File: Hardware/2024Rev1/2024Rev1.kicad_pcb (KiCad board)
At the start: 2 copper layers, 106.7 x 88.9 mm, 84 parts, among them J7 RJ45_LED_Shielded, Q2 BSS138, Q3 BSS138, Q5 BSS138, Q6 SPD30P06PGBTMA1, Q7 BSS138, U2 Opamp_Dual, U3 Teensy4.1_DEV-16771, U4 Opamp_Dual, U5 Opamp_Dual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

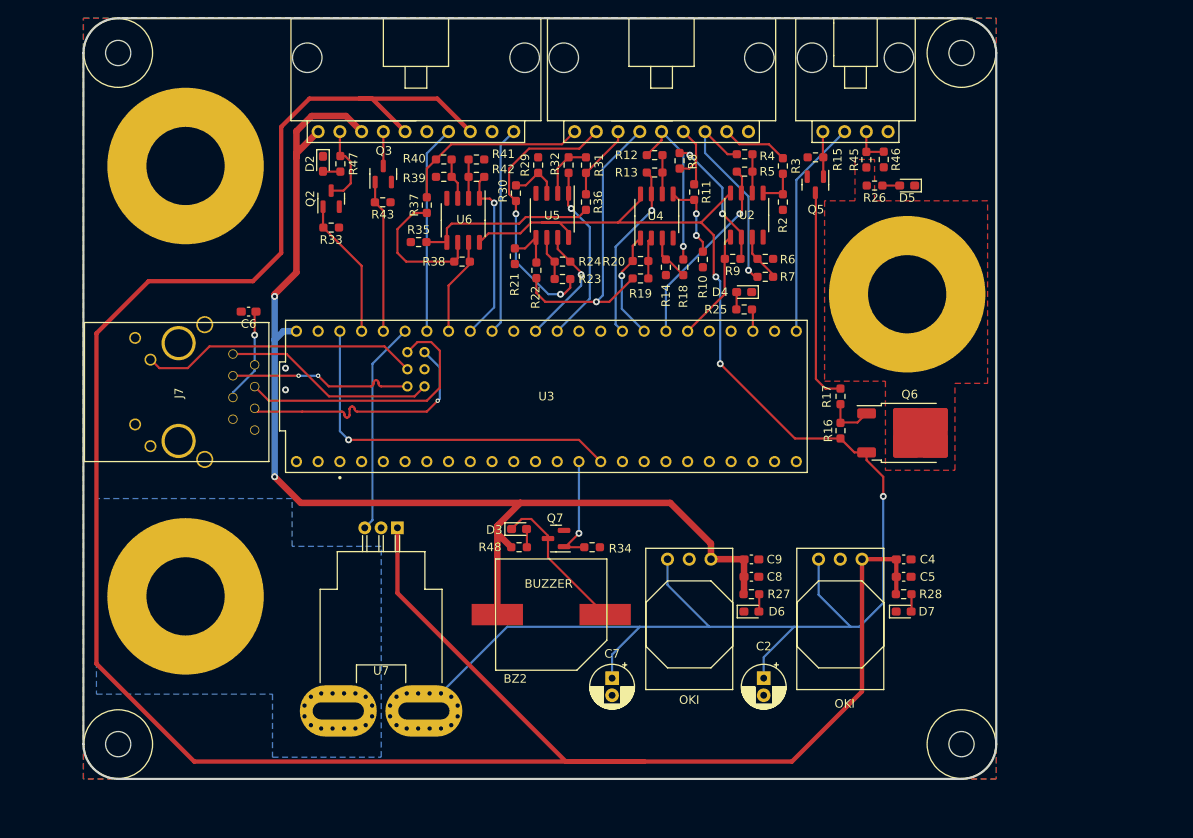
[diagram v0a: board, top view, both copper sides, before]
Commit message: added in zones for packs
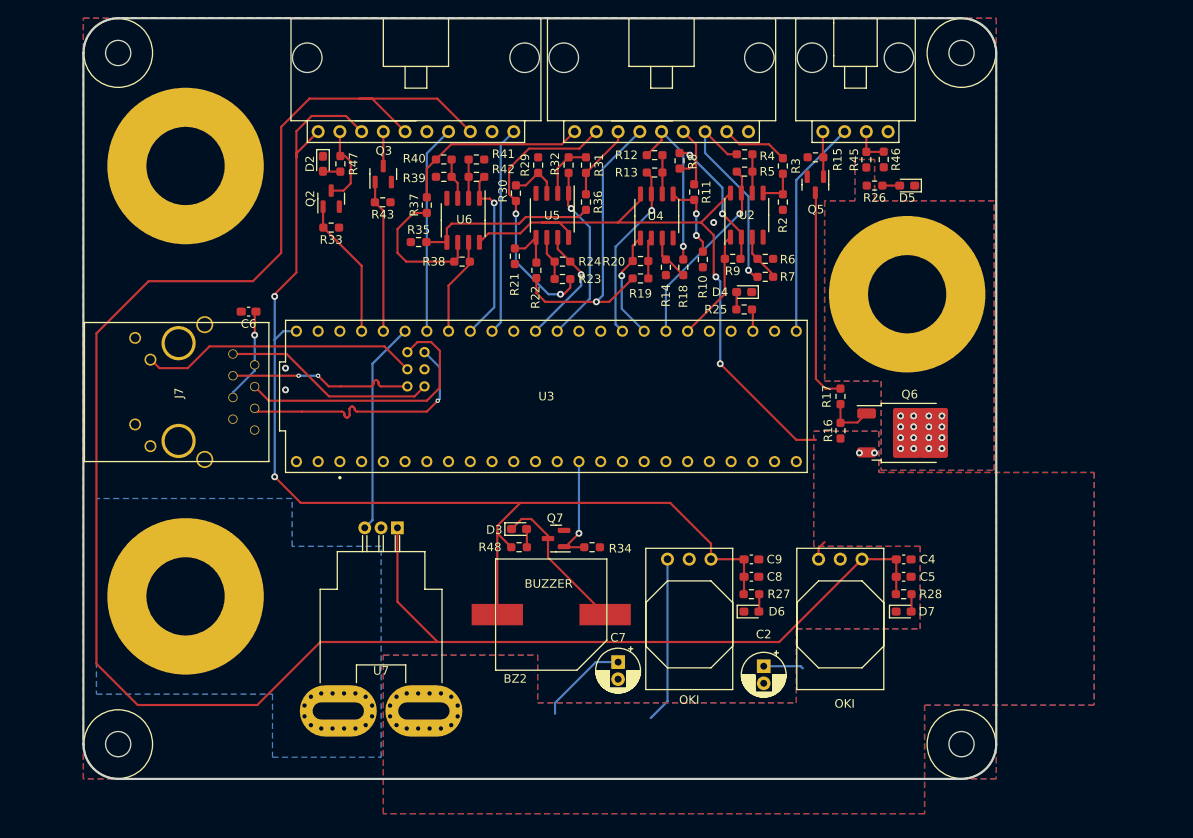
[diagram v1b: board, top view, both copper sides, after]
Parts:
- moved C7 2.01 mm to (165.4, 112.1)
- moved C2 1.40 mm to (182.4, 112.6)
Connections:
- U3 pad R-: R- -> (no net)
- U3 pad T-: T- -> (no net)
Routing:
- net PackLogic: track 190.8 -> 109.6 mm, vias 3 -> 4
- net +3.3V: track 276.6 -> 232.7 mm
- net unconnected-(U3-3.3V-Pad3.3V_1): track 43.6 -> 0.00 mm, vias 1 -> 0
- net +5V: track 139.1 -> 138.3 mm
- net PACK_OUT: vias 0 -> 16
- net GND: vias 2 -> 3
- added copper zone on B.Cu, net PACK_OUT
- added copper zone on B.Cu, net PackLogic
- added copper zone on F.Cu, net PackLogic

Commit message: enlarged board and pack zones
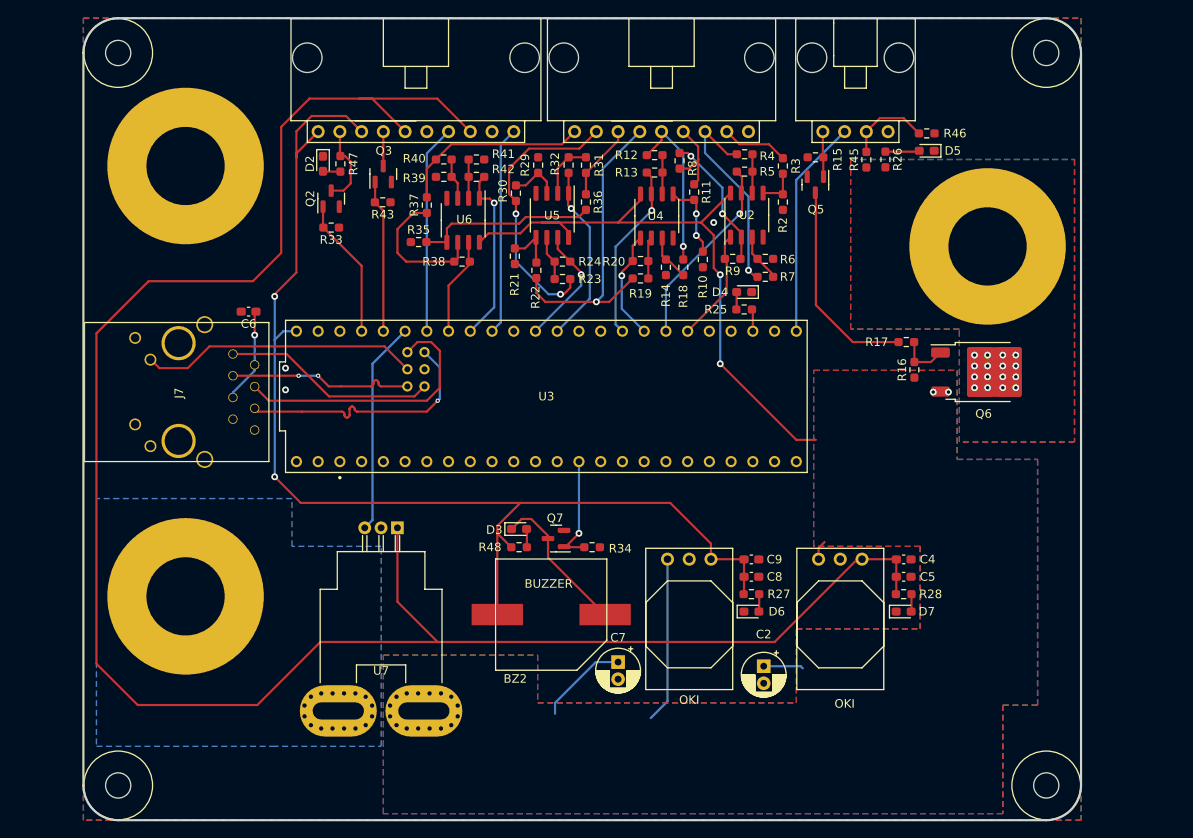
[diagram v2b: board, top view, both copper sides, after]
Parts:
- moved R16 11.2 mm to (200.0, 77.9)
- moved Q6 11.2 mm to (208.1, 78.2)
- moved H4 11.0 mm to (215.4, 126.5)
- moved V4 10.9 mm to (208.5, 63.5)
- moved R17 9.97 mm to (199.0, 74.7), turned to 180 degrees
- moved H2 9.91 mm to (215.4, 40.9)
- moved R46 5.88 mm to (201.4, 50.3), turned to 0 degrees
- moved H3 4.83 mm to (106.9, 126.5)
- moved D5 4.66 mm to (201.4, 52.3)
- moved R26 3.30 mm to (196.6, 53.3), turned to -90 degrees
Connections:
- U3 pad R-: (no net) -> R-
- U3 pad T-: (no net) -> T-
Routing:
- net Net-(Conn5-Pad3): track 4.41 -> 9.90 mm
- net Net-(D5-A): track 2.02 -> 3.99 mm
- net Net-(Q5-D): track 25.1 -> 24.6 mm
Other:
- board size 106.7 x 88.9 mm -> 116.6 x 93.7 mm

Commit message: labeld LED, added in board info, and changed zones
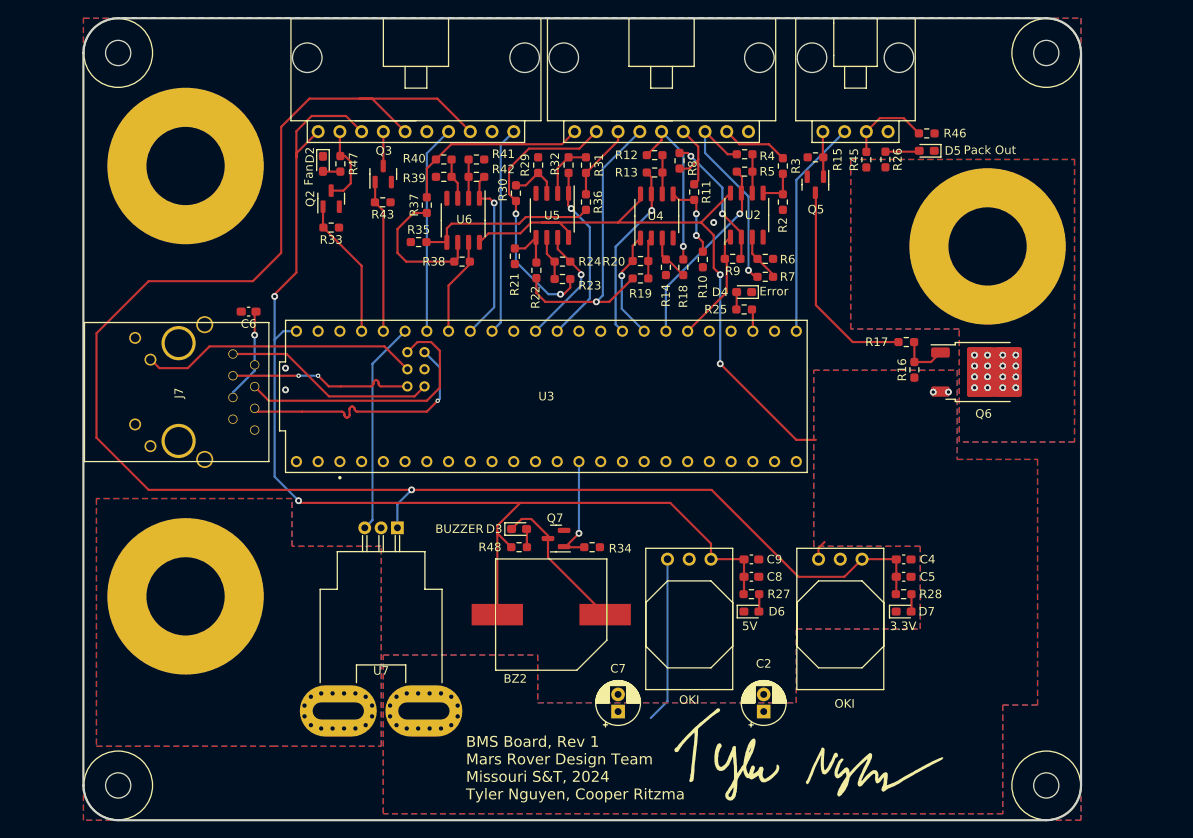
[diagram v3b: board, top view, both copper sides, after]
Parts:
- added G***: LOGO, Gimbal_Board_Library:z-sig-Tyler-Nguyen, F.Cu at (186.9, 122.9)
- moved C7 5.78 mm to (165.4, 117.9), turned to 90 degrees
- moved C2 5.30 mm to (182.4, 117.9), turned to 90 degrees
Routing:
- net +3.3V: track 232.7 -> 194.7 mm, vias 0 -> 1
- net PackLogic: track 109.6 -> 94.3 mm
- added copper zone on F.Cu, net Net-(U7-IP+)
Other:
- board text added: "3.3V"
- board text added: "5V"
- board text added: "BMS Board, Rev 1 Mars Rover Design Team Missouri S&T, 2024 Tyler Nguyen, Cooper Ritzma"
- board text added: "Error"
- board text added: "Fan"
- board text added: "Pack Out"

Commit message: Added Signature
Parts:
- added G***: LOGO, Sigtature:Signature_Cooper_Ritzma_15mmx3.5mm_mod, F.Cu at (137.7, 125.0)

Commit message: rearranged components and flags. also started on some traces
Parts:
- moved BZ2 91.0 mm to (216.6, 43.4), turned to 180 degrees
- moved R34 67.2 mm to (213.7, 55.4)
- moved R48 67.2 mm to (205.2, 55.4), turned to 0 degrees
- moved Q7 67.2 mm to (209.5, 54.4)
- moved D3 67.1 mm to (205.2, 53.3), turned to 180 degrees
- moved G*** 53.2 mm to (190.2, 116.8)
- moved J7 48.2 mm to (116.5, 35.0), turned to 180 degrees
- moved D7 47.0 mm to (212.6, 61.3), turned to 90 degrees
- moved R28 44.2 mm to (209.6, 61.3), turned to -90 degrees
- moved V4 43.7 mm to (200.4, 106.4)
- moved D6 43.4 mm to (212.9, 76.8), turned to 90 degrees
- moved C5 41.5 mm to (206.5, 61.3), turned to 90 degrees
- moved R27 39.6 mm to (209.6, 76.8), turned to -90 degrees
- moved C4 39.0 mm to (203.5, 61.3), turned to 90 degrees
- moved R16 36.8 mm to (169.2, 98.0)
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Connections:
- Conn3 pad 4: cell4 -> cell5
- Conn3 pad 5: cell5 -> cell4
- Conn3 pad 6: cell6 -> cell7
- Conn3 pad 7: cell7 -> cell6
- U3 pad 12: Buzzer-Teensy -> unconnected-(U3-MISO-Pad12)
- U3 pad 21: CURRENT_SENSE -> unconnected-(U3-A7-Pad21)
- U3 pad 24: unconnected-(U3-A10-Pad24) -> CURRENT_SENSE
- U3 pad 33: GATE -> ERR_LED
- U3 pad 34: unconnected-(U3-RX8-Pad34) -> Buzzer-Teensy
- U3 pad 35: ERR_LED -> GATE
- U3 pad R-: R- -> (no net)
- U3 pad T-: T- -> (no net)
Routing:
- net +3.3V: track 194.7 -> 0.00 mm, vias 1 -> 0
- net +5V: track 138.3 -> 0.00 mm, vias 2 -> 0
- net PackLogic: track 94.3 -> 40.6 mm, vias 4 -> 0
- net cell4: track 36.5 -> 3.49 mm, vias 1 -> 0
- net LED: track 32.6 -> 0.00 mm
- net R+: track 32.0 -> 0.00 mm
- net R-: track 30.5 -> 0.00 mm, vias 1 -> 0
- net GATE: track 25.7 -> 0.00 mm
- net CURRENT_SENSE: track 24.9 -> 0.00 mm
- net T+: track 24.9 -> 0.00 mm
- net Net-(Q5-D): track 24.6 -> 0.00 mm
- net cell7: track 24.5 -> 0.00 mm, vias 1 -> 0
- net Cell8-SENSE: track 22.6 -> 0.00 mm, vias 1 -> 0
- net T-: track 21.8 -> 0.00 mm, vias 2 -> 0
- net Cell6-SENSE: track 20.9 -> 2.66 mm, vias 1 -> 0
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- removed copper zone on B.Cu, net Net-(U7-IP+)
- removed copper zone on F.Cu, net Net-(U7-IP+)
- removed copper zone on B.Cu, net PACK_OUT
- removed copper zone on F.Cu, net PACK_OUT
- removed copper zone on B.Cu, net PackLogic
- removed copper zone on F.Cu, net PackLogic
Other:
- board size 116.6 x 93.7 mm -> 135.1 x 90.7 mm

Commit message: did more traces
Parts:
- Q6: footprint Package_TO_SOT_SMD:TO-252-2 -> Package_TO_SOT_SMD:TO-263-7_TabPin4
- moved Q6 7.82 mm to (182.9, 102.9)
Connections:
- U3 pad 38: Cell7-SENSE -> Cell8-SENSE
- U3 pad 39: Cell8-SENSE -> Cell7-SENSE
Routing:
- net +5V: track 0.00 -> 208.8 mm
- net +3.3V: track 0.00 -> 183.1 mm
- net Net-(Q5-D): track 0.00 -> 49.2 mm, vias 0 -> 2
- net CURRENT_SENSE: track 0.00 -> 34.1 mm
- net Buzzer-Teensy: track 0.00 -> 33.5 mm, vias 0 -> 1
- net PackLogic: track 40.6 -> 69.1 mm
- net cell6: track 0.00 -> 26.4 mm, vias 0 -> 2
- net GATE: track 0.00 -> 25.3 mm
- net cell8: track 0.00 -> 25.2 mm, vias 0 -> 1
- net Cell7-SENSE: track 0.00 -> 19.7 mm, vias 0 -> 1
- net cell2: track 6.13 -> 25.7 mm, vias 0 -> 2
- net cell4: track 3.49 -> 22.7 mm, vias 0 -> 2
- net Net-(U2B-+): track 0.00 -> 15.0 mm
- net Net-(BZ2-+): track 0.00 -> 13.8 mm
- net cell7: track 0.00 -> 13.1 mm
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- added copper zone on B.Cu, net Net-(U7-IP+)
- added copper zone on F.Cu, net Net-(U7-IP+)
- added copper zone on B.Cu, net PackLogic
- added copper zone on F.Cu, net PackLogic

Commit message: redid ethernet traces
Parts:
- Q6: footprint Package_TO_SOT_SMD:TO-263-7_TabPin4 -> Package_TO_SOT_SMD:TO-263-7_TabPin8
- moved R33 0.25 mm to (131.8, 62.5)
- moved Q2 0.25 mm to (131.8, 58.2)
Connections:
- net PackLogic renamed Pack
- U3 pad R-: (no net) -> R-
- U3 pad T-: (no net) -> T-
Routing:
- net T+: track 0.00 -> 68.6 mm
- net T-: track 0.00 -> 68.4 mm
- net LED: track 0.00 -> 51.6 mm
- net R-: track 0.00 -> 44.3 mm
- net R+: track 0.00 -> 44.2 mm
- net +5V: track 208.8 -> 231.7 mm
- net Net-(C6-Pad1): track 0.00 -> 12.7 mm
- net Fan: track 11.3 -> 9.85 mm
- net GND: vias 0 -> 2

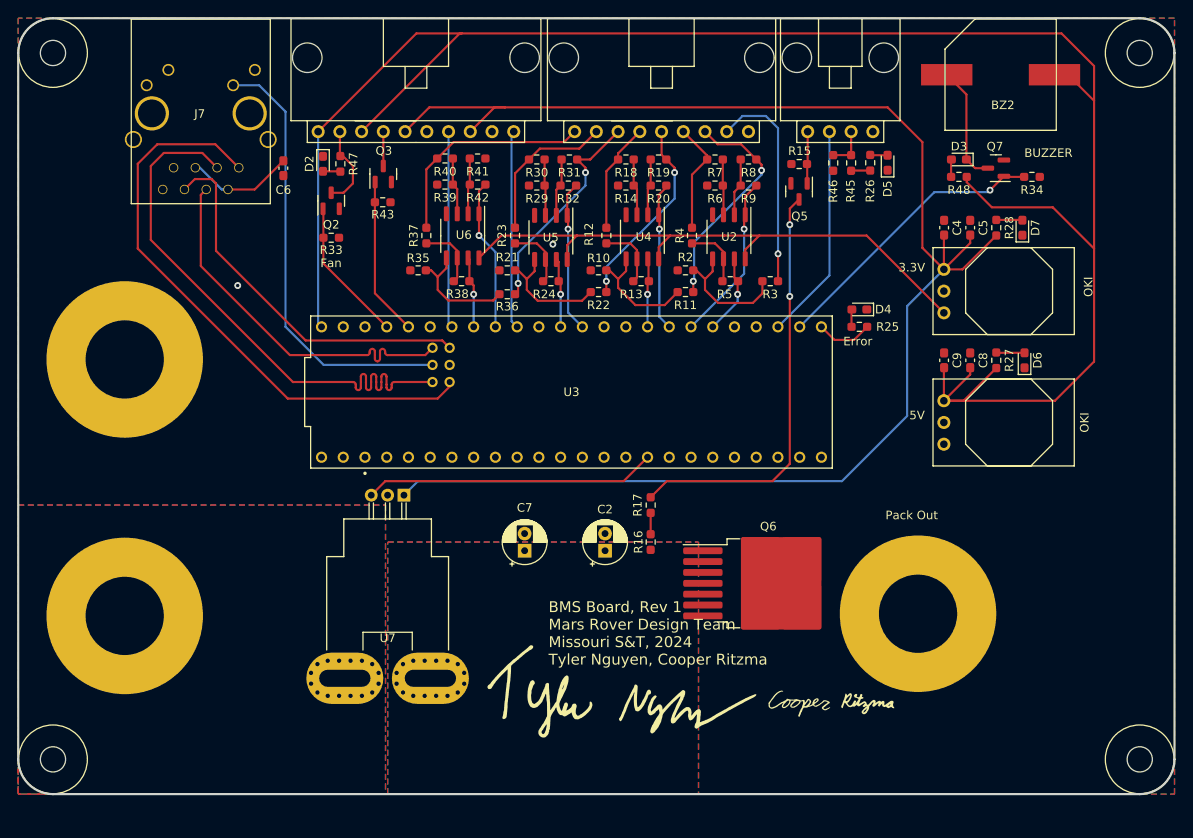
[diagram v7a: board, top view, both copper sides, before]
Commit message: redid zones and added in vias for zones
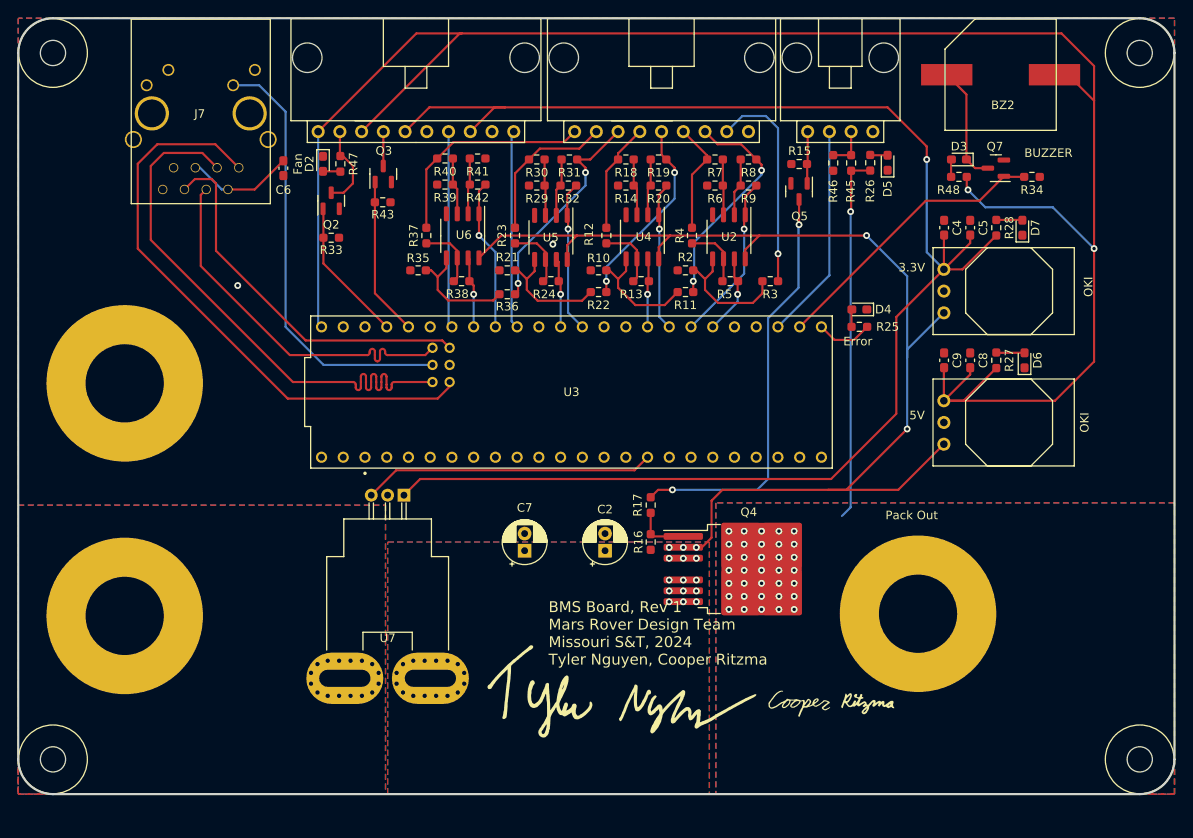
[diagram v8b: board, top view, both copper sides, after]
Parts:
- removed Q6: SPD30P06PGBTMA1, Package_TO_SOT_SMD:TO-263-7_TabPin8
- added Q4: IPB180N10S4-02, Package_TO_SOT_SMD:TO-263-6, F.Cu at (180.6, 101.2)
- moved V2 2.79 mm to (107.7, 79.5)
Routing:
- net Pack: track 69.1 -> 138.1 mm, vias 0 -> 17
- net PACK_OUT: track 2.24 -> 43.0 mm, vias 0 -> 36
- net Net-(Q4-G): track 2.49 -> 6.41 mm
- net +3.3V: track 183.1 -> 182.2 mm, vias 0 -> 1
- net +5V: track 231.7 -> 232.2 mm, vias 0 -> 2
- net Buzzer-Teensy: vias 1 -> 0
- added copper zone on B.Cu, net PACK_OUT
- added copper zone on F.Cu, net PACK_OUT
